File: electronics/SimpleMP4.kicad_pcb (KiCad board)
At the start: 2 copper layers, 136.9 x 66.4 mm, 130 parts, among them J1 USB_OTG, J2 DISPLAY, Q1 8050, Q2 SI2305, Q3 SI2305, Q4 8050, Q5 8550, Q6 SI2305, Q7 8550, U1 OCP8020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

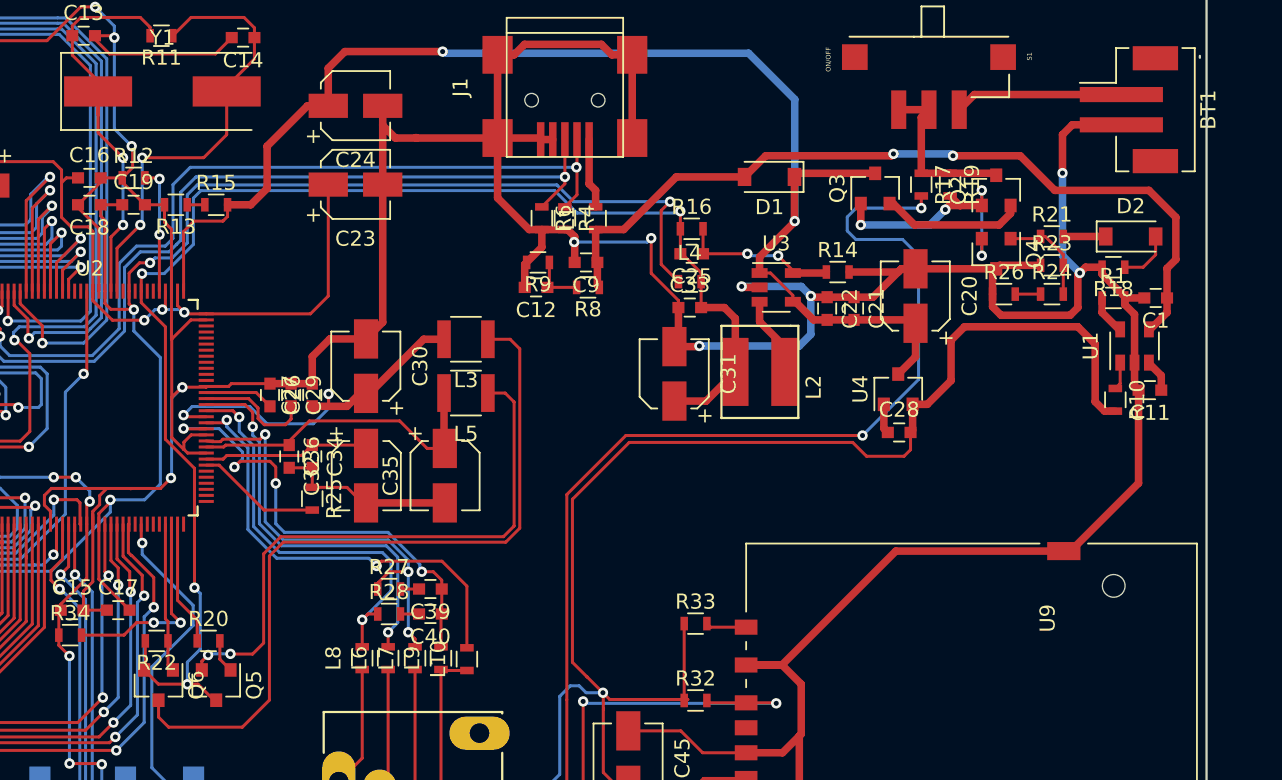
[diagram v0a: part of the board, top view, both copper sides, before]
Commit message: routed most connections
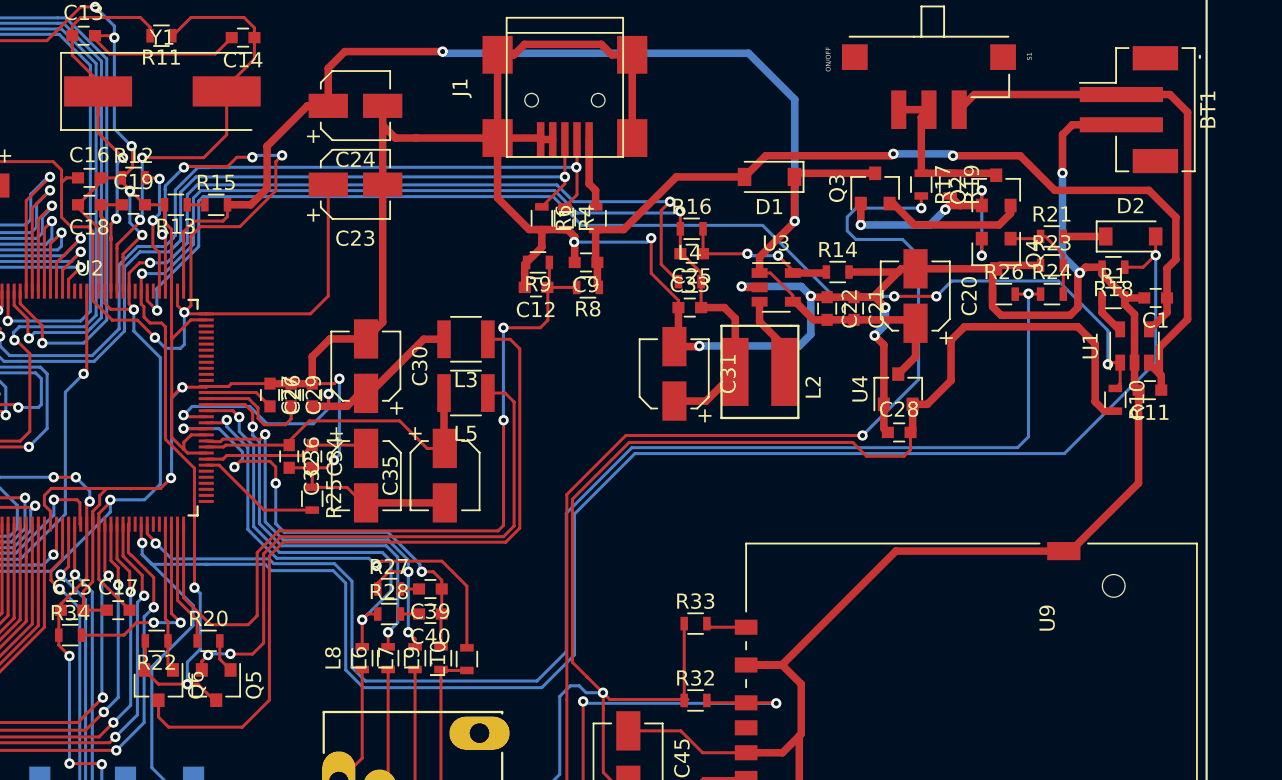
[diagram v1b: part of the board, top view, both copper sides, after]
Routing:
- net /PLAY_ON: track 25.4 -> 121.0 mm, vias 1 -> 2
- net /PWR_ON: track 1.68 -> 89.6 mm, vias 0 -> 2
- net /CHG_OK: track 1.84 -> 79.6 mm, vias 0 -> 4
- net /USB_DET: track 3.63 -> 53.9 mm, vias 0 -> 2
- net VCC: track 420.8 -> 452.7 mm, vias 23 -> 26
- net GND: track 578.7 -> 604.8 mm, vias 24 -> 30
- net /VB: track 13.3 -> 36.2 mm

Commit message: done routing
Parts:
- moved C46 182.8 mm to (68.6, 143.1)
- moved C47 177.0 mm to (68.6, 144.5)
- moved C44 173.3 mm to (68.6, 146.1)
- moved U5 59.0 mm to (164.1, 162.3)
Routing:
- net GND: track 604.8 -> 839.4 mm, vias 30 -> 47
- net /DQM1: track 0.00 -> 117.6 mm, vias 0 -> 8
- net /DQM0: track 0.00 -> 101.6 mm, vias 0 -> 6
- net VCC: track 452.7 -> 502.5 mm, vias 26 -> 31
- net /RESETN: track 84.5 -> 112.2 mm, vias 4 -> 6
- net /FCE0: track 39.8 -> 38.1 mm
- net /XOUT: track 27.2 -> 25.6 mm
- net /D9: track 115.1 -> 113.9 mm
- net /D10: track 114.6 -> 113.7 mm
- net /D8: track 115.2 -> 114.4 mm
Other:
- board size 136.9 x 66.4 mm -> 136.9 x 66.9 mm

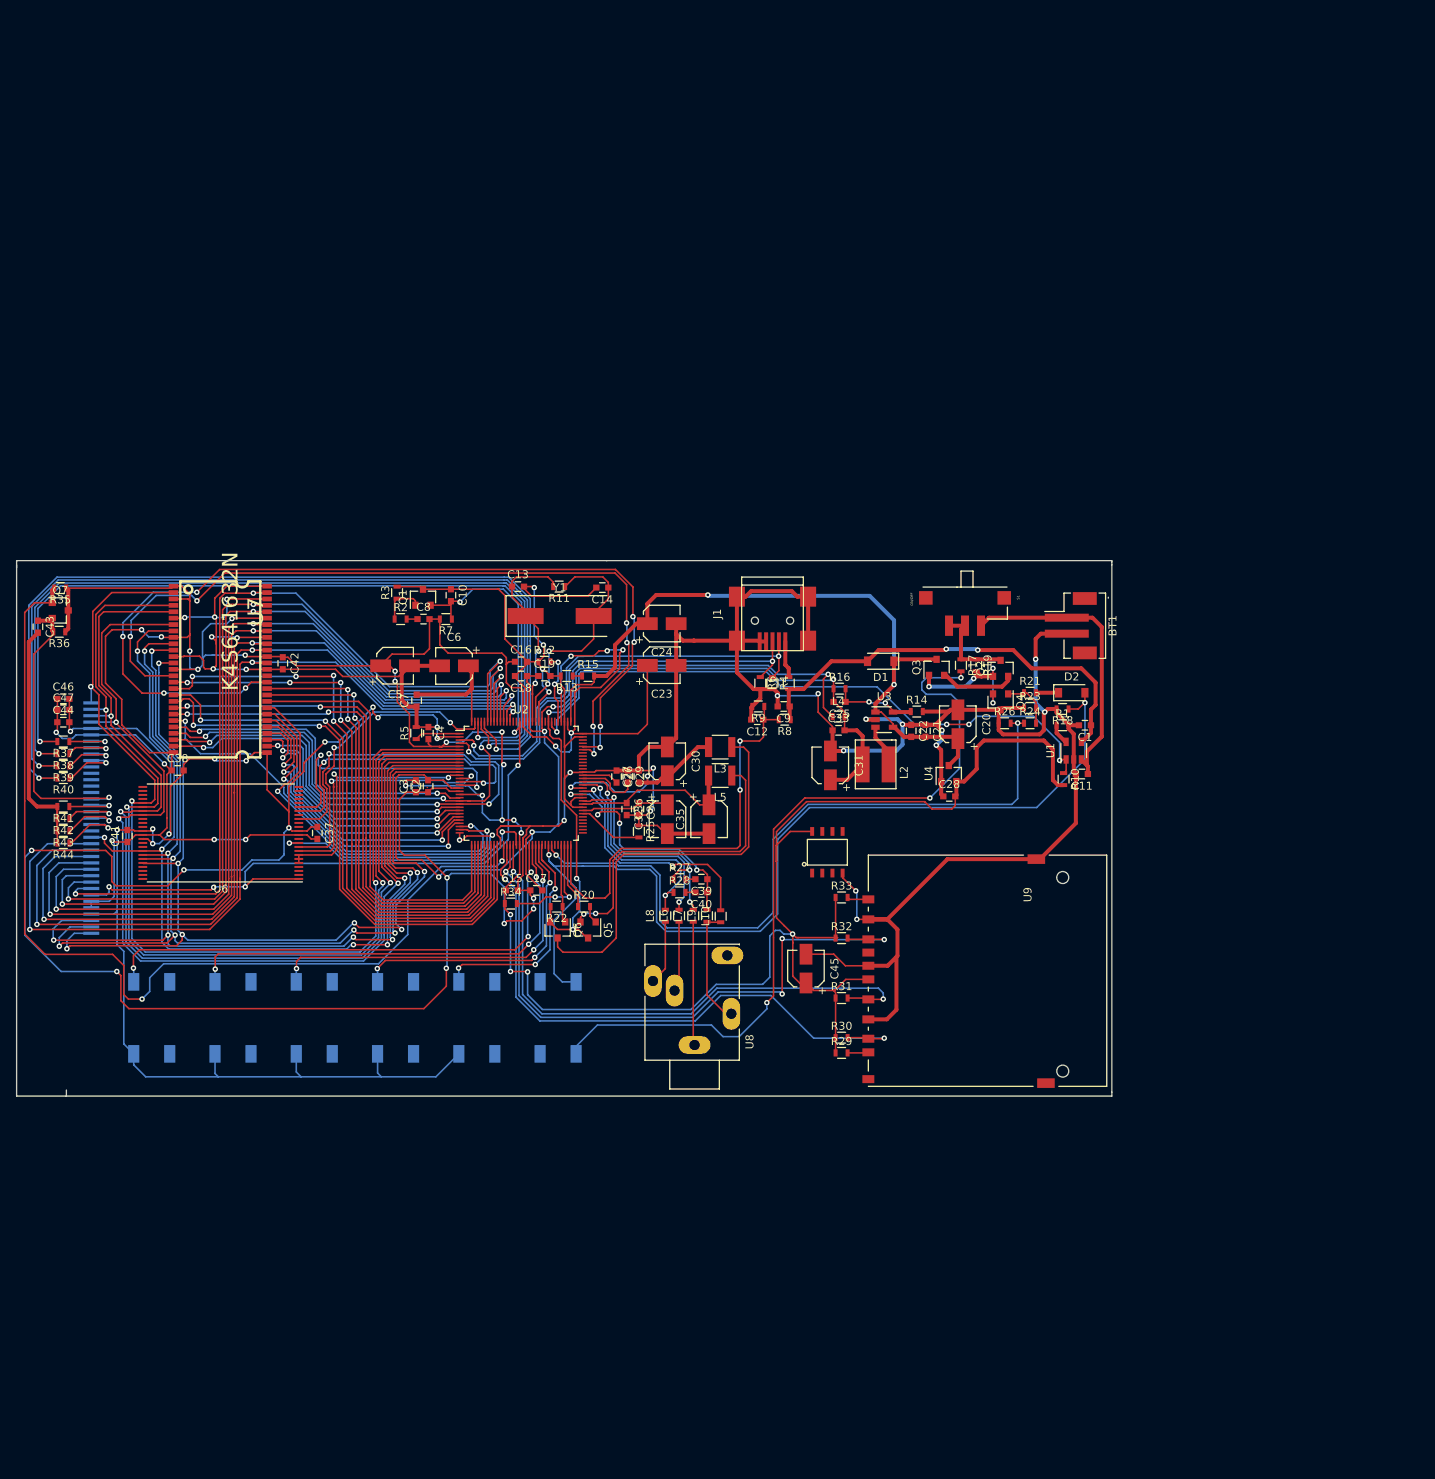
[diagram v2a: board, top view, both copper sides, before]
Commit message: added filled zones
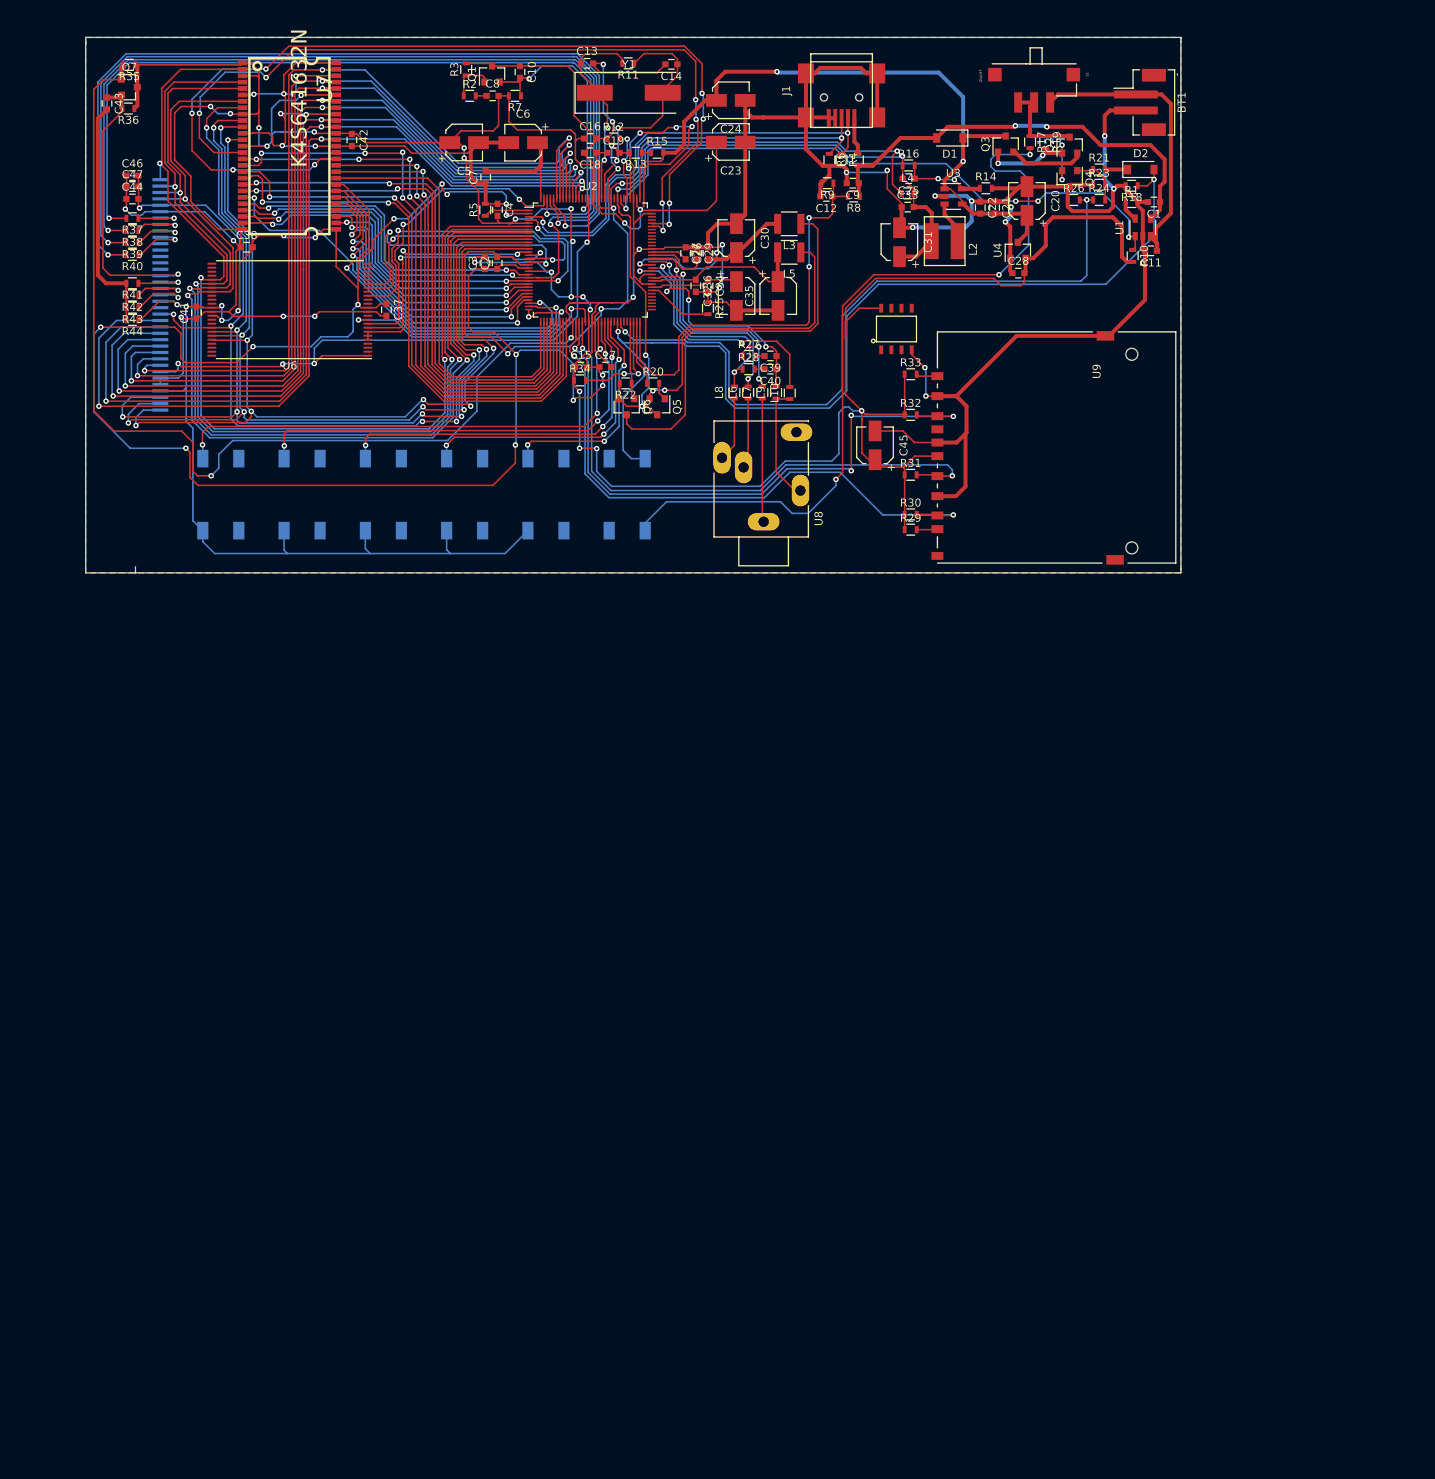
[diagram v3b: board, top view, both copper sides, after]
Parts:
- moved L8 66.0 mm to (152.5, 104.8)
- moved R12 66.0 mm to (137.4, 73.1)
- moved R20 66.0 mm to (142.3, 103.7)
- moved R22 66.0 mm to (138.9, 103.7)
- moved R34 66.0 mm to (133.2, 103.3)
- moved S1 66.0 mm to (189.9, 67.1)
- moved U2 66.0 mm to (134.5, 88.3)
- moved B3 66.0 mm to (118.7, 117.6)
- moved BT1 66.0 mm to (203.8, 68.6)
- moved C1 66.0 mm to (204.9, 81.0)
- moved C10 66.0 mm to (125.7, 64.8)
- moved C16 66.0 mm to (134.4, 73.1)
- moved C19 66.0 mm to (137.4, 74.9)
- moved C21 66.0 mm to (185.0, 81.7)
- moved C26 66.0 mm to (146.4, 87.4)
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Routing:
- added copper zone on B.Cu, net GND
- added copper zone on F.Cu, net GND
